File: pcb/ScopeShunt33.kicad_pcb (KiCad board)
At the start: 2 copper layers, 50 x 50 mm, 35 parts, among them J1 Screw_Terminal_01x02, J2 Conn_Coaxial

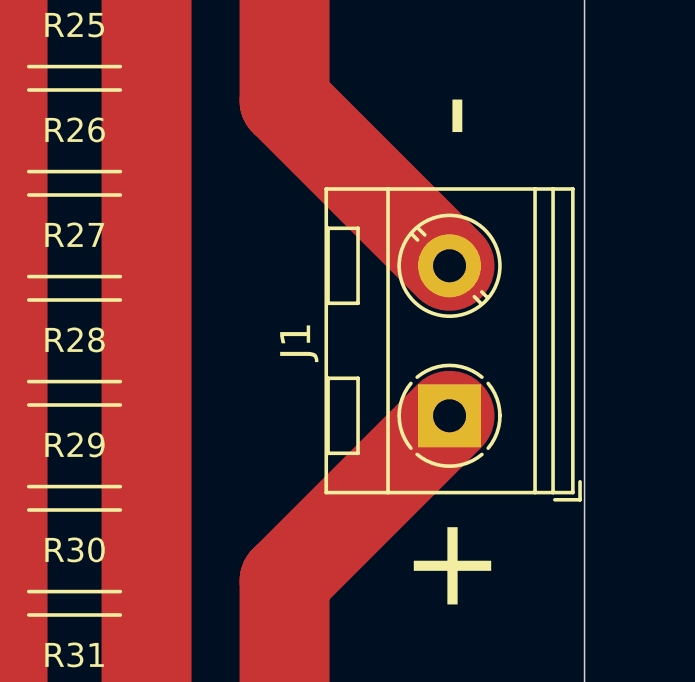
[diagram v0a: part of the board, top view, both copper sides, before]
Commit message: screw terminal footprint
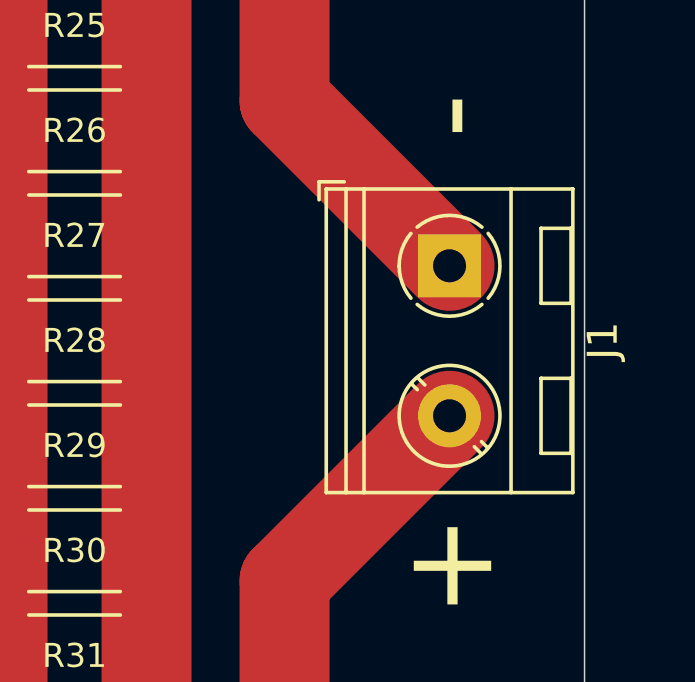
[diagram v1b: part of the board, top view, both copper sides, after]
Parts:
- moved J1 5.00 mm to (170.5, 97.5), turned to 270 degrees
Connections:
- J1 pad 1: /+ -> /-
- J1 pad 2: /- -> /+
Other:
- board text added: "v002"
- board text removed: "v001"
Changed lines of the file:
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@@
   )
   (setup
-    (last_trace_width 3)
+    (last_trace_width 0.25)
     (user_trace_width 0.2)
     (user_trace_width 2)
@@
     (pad_to_mask_clearance 0)
     (aux_axis_origin 0 0)
+    (grid_origin 151 100)
     (visible_elements FFFFFF7F)
     (pcbplotparams
@@
       (drillshape 0)
       (scaleselection 1)
-      (outputdirectory "GERBER_ScopeShunt33_v001"))
+      (outputdirectory "GERBER_ScopeShunt33_v002"))
   )
   (net 0 "")
@@
   )
   (module 000_LOCAL:TerminalBlock_RND_205-00045_1x02_P5.00mm_Horizontal (layer F.Cu)
-    (at 170.5 102.5 90)
+    (at 170.5 97.5 270)
     (descr "terminal block RND 205-00045, 2 pins, pitch 5mm, size 10x8.1mm^2, drill diamater 1.1mm, pad diameter 2.1mm, see http://cdn-reichelt.de/documents/datenblatt/C151/RND_205-00045_DB_EN.pdf, script-generated using https://github.com/pointhi/kicad-footprint-generator/scripts/TerminalBlock_RND")
     (tags "THT terminal block RND 205-00045 pitch 5mm size 10x8.1mm^2 drill 1.1mm pad 2.1mm")
@@
     (fp_arc (start 0 0) (end 1.287 1.08) (angle -80) (layer F.SilkS) (width 0.12))
     (fp_arc (start 0 0) (end 0 1.68) (angle -40) (layer F.SilkS) (width 0.12))
-    (pad 2 thru_hole circle (at 5 0 90) (size 2.1 2.1) (drill 1.1) (layers *.Cu *.Mask)
-      (net 1 /-))
-    (pad 1 thru_hole rect (at 0 0 90) (size 2.1 2.1) (drill 1.1) (layers *.Cu *.Mask)
-      (net 2 /+))
+    (pad 2 thru_hole circle (at 5 0 270) (size 2.1 2.1) (drill 1.1) (layers *.Cu *.Mask)
+      (net 2 /+))
+    (pad 1 thru_hole rect (at 0 0 270) (size 2.1 2.1) (drill 1.1) (layers *.Cu *.Mask)
+      (net 1 /-))
     (model ${KIPRJMOD}/000_LOCAL.pretty/3d/TerminalBlock_Phoenix_MKDS-1,5-2_1x02_P5.00mm_Horizontal.step
       (at (xyz 0 0 0))
@@
     (effects (font (size 1 1) (thickness 0.15)) (justify mirror))
   )
-  (gr_text v001 (at 150 78.75) (layer B.SilkS)
+  (gr_text v002 (at 150 78.75) (layer B.SilkS)
     (effects (font (size 1 1) (thickness 0.15)) (justify mirror))
   )
